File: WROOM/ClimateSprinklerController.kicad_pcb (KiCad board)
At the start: 2 copper layers, 136 x 100 mm, 187 parts, among them J1 7.5 TO 40 V, J10 DISPLAY_2, J11 HVAC, J12 RELAY, J2 POWER SEL, J3 EXT_ENC, J4 SERIAL, J5 SPI, J6 I2C, J7 PIR, J8 IO_EXP, J9 DISPLAY_1, K1 G5Q-1-DC5, K2 G5Q-1-DC5, K3 G5Q-1-DC5, Q1 TEPT5700, Q10 2N6073B, Q11 2N6073B, Q12 2N6073B, Q13 2N6073B, Q2 2N7002, Q3 2N7002, Q4 2N7002, Q5 2N7002, Q6 2N6073B, Q7 2N6073B, Q8 2N6073B, Q9 2N6073B, SW1 RESET, SW2 MODE, SW3 PEC11S-929K-S0015, U1 ESP32-WROOM-32D, U10 MOC3043, U11 MOC3043, U12 MOC3043, U13 MOC3043, U14 MOC3043, U15 MOC3043, U16 MOC3043, U2 MCP23017_SO, U3 LMR36520, U4 LD1086DT33TR, U5 TMP117, U6 DHT22, U7 BME280, U8 SHTC3, U9 MOC3043

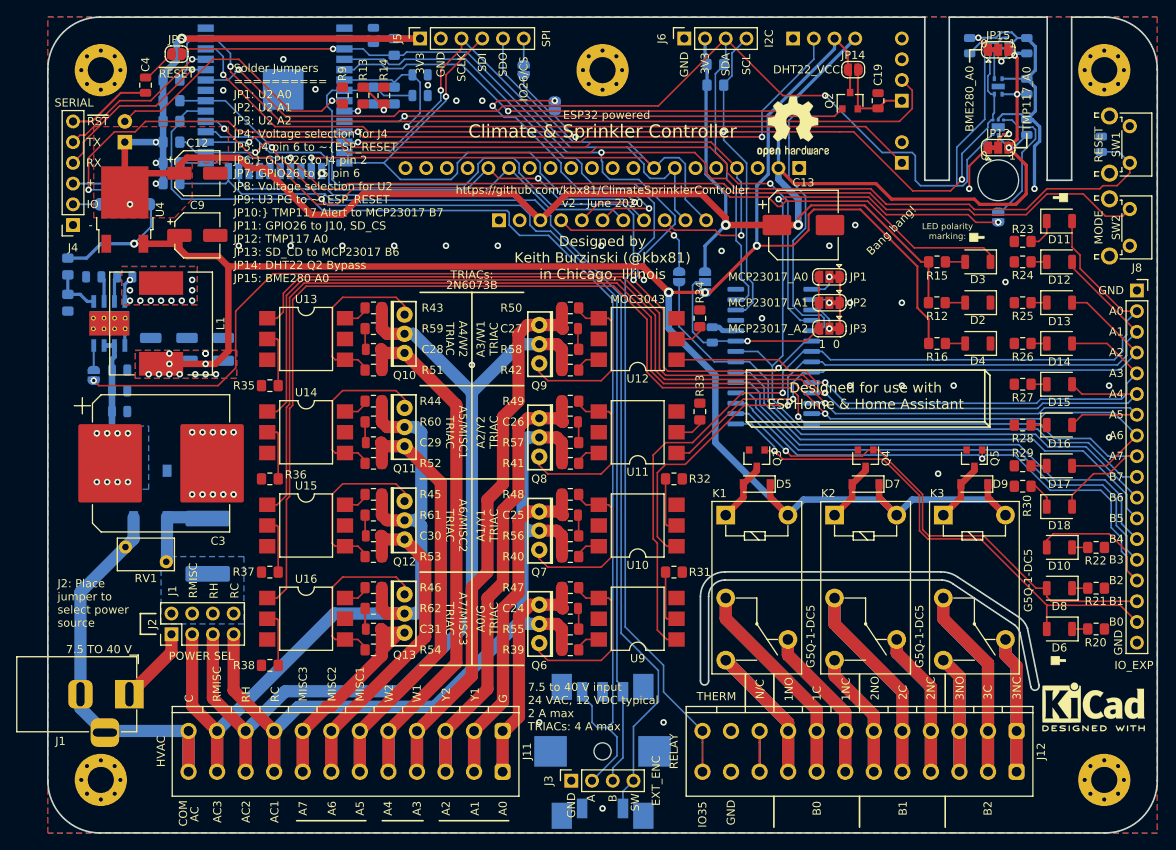
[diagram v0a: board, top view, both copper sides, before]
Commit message: Doc updates, new images, new enclosures, regenerate gerbers
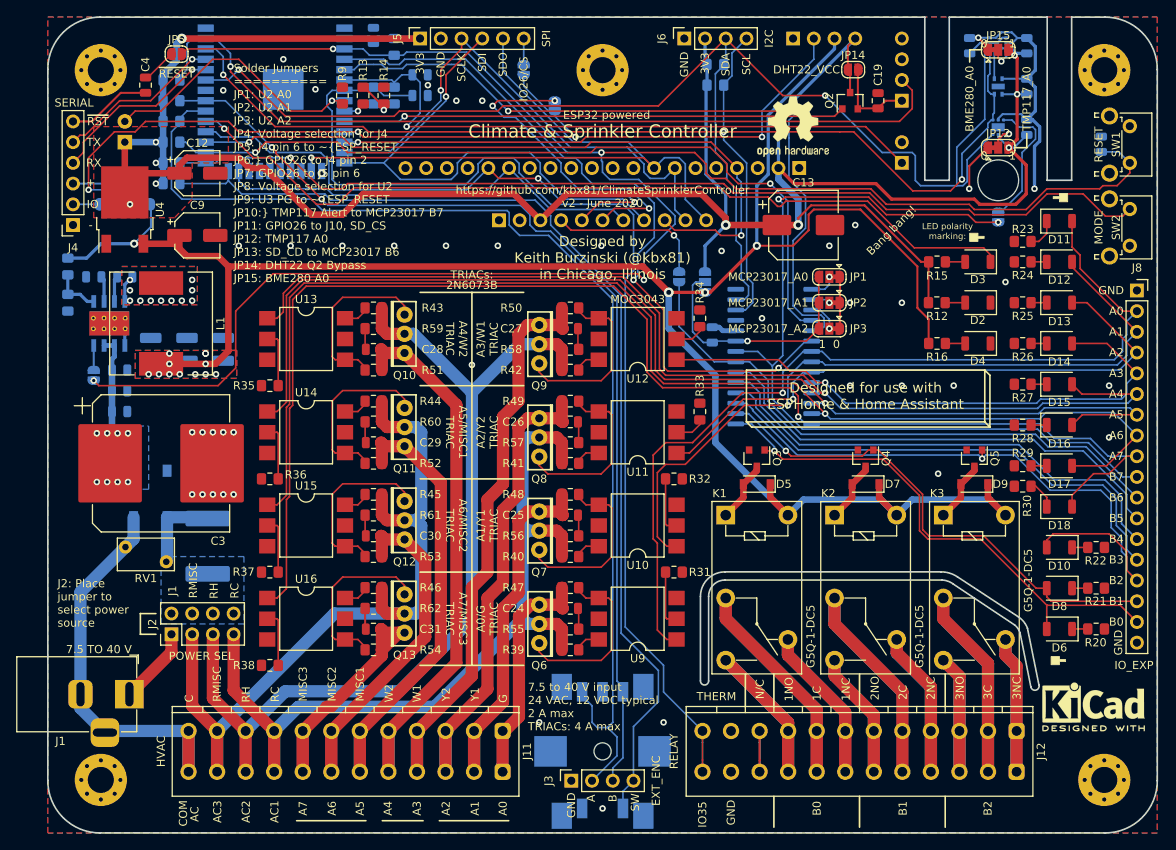
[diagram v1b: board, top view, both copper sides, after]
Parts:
- D1: value CD-MBL206SL -> N/A
- D5, D7, D9: value 1N4148 -> N/A
- F1: value 1.5A -> 300 mA
- R20, R21, R22: value 1K2 -> 560
- R23: value 9K1 -> 10K
- R24, R25, R28, R29, R30: value 2K7 -> 1K5
- RV1: value B72205S0400K101 -> N/A
- TH1: value NXFT15XH103FA2B100 -> 10K
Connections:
- JP14 pad 1: +5V -> +3V3
- Q2 pad 3: +5V -> +3V3
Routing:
- net +5V: track 266.2 -> 258.8 mm
- net +3V3: track 316.2 -> 323.3 mm
